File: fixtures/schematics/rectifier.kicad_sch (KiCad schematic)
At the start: 9 parts

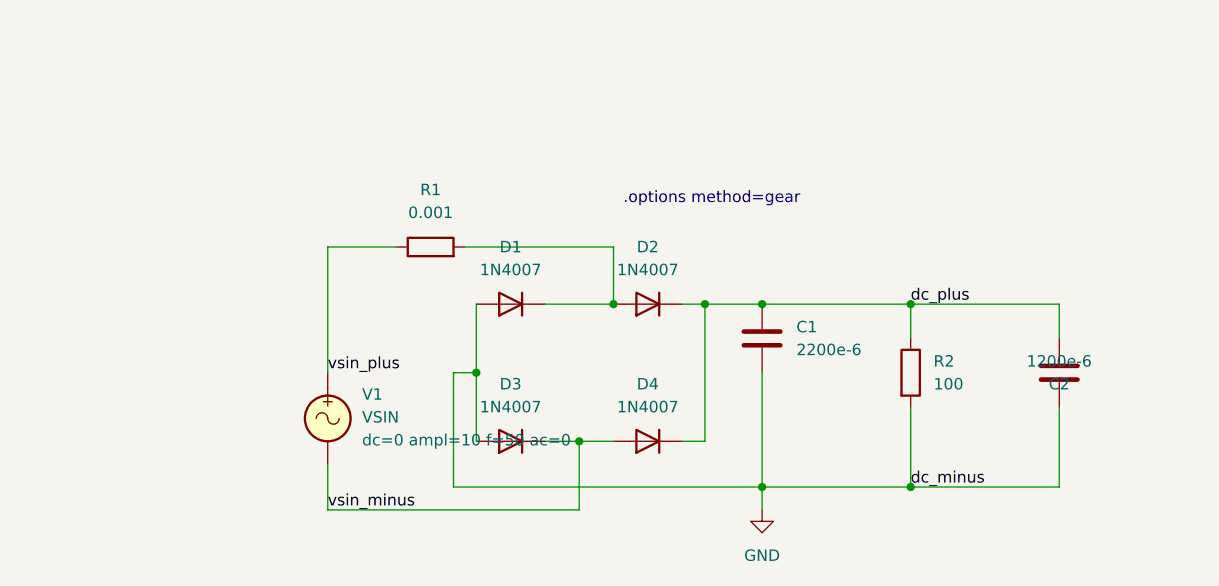
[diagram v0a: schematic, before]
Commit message: feat: simulation ingestion pipeline + SPICE library context
## Core Features

### Simulation Ingestion (Phase 2)
- CSV file parsing with waveform statistics
- Console output parsing (ngspice format)
- Analysis type detection (tran, ac, dc, op)
- FIFO archive (keeps last 5 runs)

### SPICE Library Context
- Extract Sim.Library properties from components
- Load complete .lib files (comments stripped)
- Expose subcircuits and models to LLM context
- Enable topology reasoning (antiparallel diode detection)

### Session Management
- Project-scoped persistence (.hephaistus/)
- Session restore auto-discovery
- SQLite history store for conversation
- Schematic hash for staleness detection

### API Endpoints
- POST /api/schematic/load - Load and parse schematic
- POST /api/simulation/import - Import CSV/console
- GET /api/session/status - Session + SPICE libraries
- GET /api/simulation/state - Freshness status
- GET /api/context/assemble - Full LLM context

## Fixes
- Parser: Extract lib_id, value from symbol_instances
- Parser: Filter #PWR* power symbols
- Session layer: Detailed component pin-net mapping
- Staleness: Compare schematic hashes properly

## Test Results
- Tests 14-19 passing (SPICE context, simulation import, LLM query)
- Test 18 clarified: staleness is per-project (different project = new session)
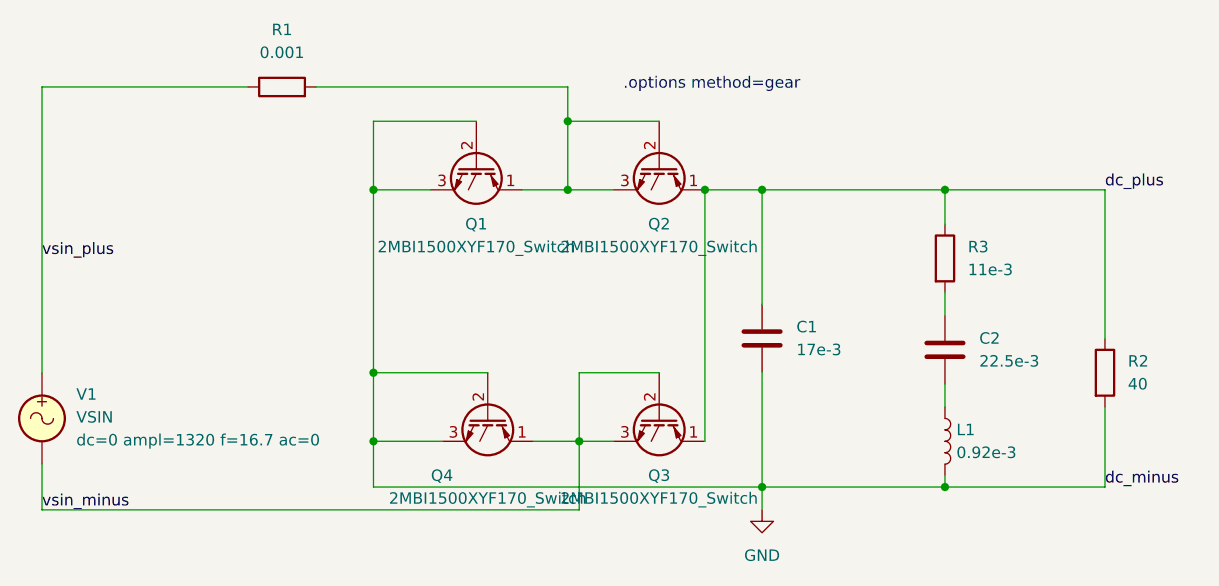
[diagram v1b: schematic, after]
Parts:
- removed D1, D2, D3, D4: 1N4007, Diode_THT:D_DO-41_SOD81_P10.16mm_Horizontal, symbol Diode:1N4007
- added L1: 0.92e-3, symbol Device:L
- added Q1, Q2, Q3, Q4: 2MBI1500XYF170_Switch, symbol Traction_Power_Components:2MBI1500XYF170_Switch
- added R3: 11e-3, symbol Device:R
- C1: value 2200e-6 -> 17e-3
- C2: value 1200e-6 -> 22.5e-3
- R2: value 100 -> 40
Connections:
- net GND: now also L1.2, Q1.2 (G), Q1.3 (E), Q4.2 (G), Q4.3 (E); no longer C2.2
- net dc_plus: now also Q2.1 (C), Q3.1 (C), R3.1; no longer C2.1
- net vsin_minus: now also Q3.2 (G), Q3.3 (E), Q4.1 (C)
- net at R1.2: now also Q1.1 (C), Q2.2 (G), Q2.3 (E)
- new net: C2.1, R3.2
- new net: C2.2, L1.1
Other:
- moved on the sheet: R2, V1
